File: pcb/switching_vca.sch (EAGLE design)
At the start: 38 parts, among them Q101 PMOS, Q102 NJFET, U101 LM319, U102 LF353D, U103 LF353D, U701 V_REG_LDOSMD

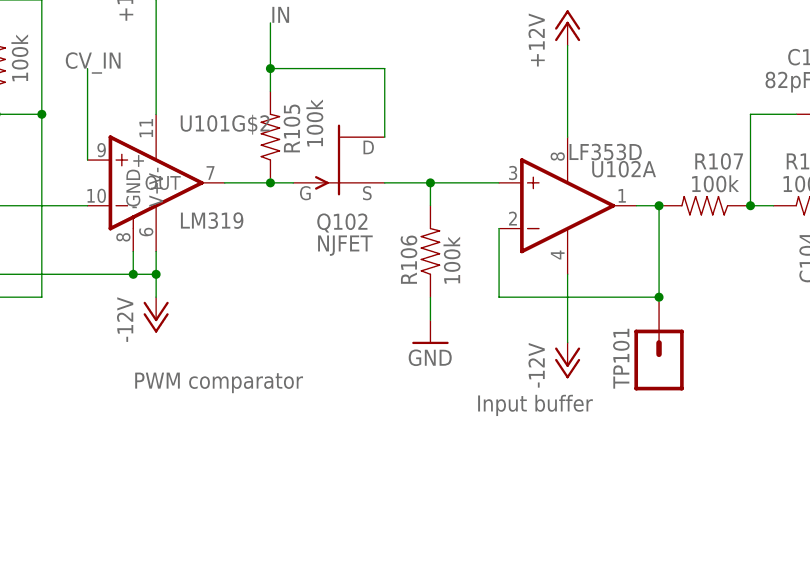
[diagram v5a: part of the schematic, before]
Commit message: added test point for PWM comparator output
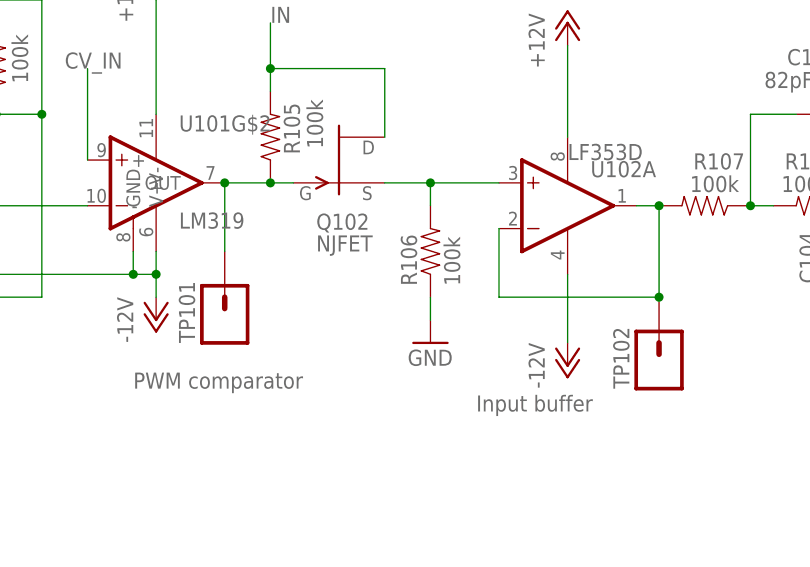
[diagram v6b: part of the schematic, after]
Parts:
- added TP102: M01PTH, SparkFun:M01PTH
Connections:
- net N$15: now also TP102.1; no longer TP101.1
- net N$3: now also TP101.1
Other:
- moved on the sheet: TP101
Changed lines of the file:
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@@
 <setting verticaltext="up"/>
 </settings>
-<grid distance="0.1" unitdist="inch" unit="inch" style="lines" multiple="1" display="yes" altdistance="0.01" altunitdist="inch" altunit="inch"/>
+<grid distance="0.1" unitdist="inch" unit="inch" style="lines" multiple="1" display="no" altdistance="0.01" altunitdist="inch" altunit="inch"/>
 <layers>
 <layer number="1" name="Top" color="4" fill="1" visible="no" active="no"/>
@@
 <part name="U701" library="SparkFun" deviceset="V_REG_LDO" device="SMD"/>
 <part name="U101" library="russruss" deviceset="LM319" device=""/>
+<part name="TP102" library="SparkFun" deviceset="M01" device="PTH" value=""/>
 <part name="TP101" library="SparkFun" deviceset="M01" device="PTH" value=""/>
 </parts>
@@
 <instance part="U101" gate="G$2" x="73.66" y="121.92"/>
 <instance part="U101" gate="G$3" x="73.66" y="121.92"/>
-<instance part="TP101" gate="G$1" x="129.54" y="101.6" rot="R90"/>
+<instance part="TP102" gate="G$1" x="129.54" y="101.6" rot="R90"/>
+<instance part="TP101" gate="G$1" x="81.28" y="106.68" rot="R90"/>
 </instances>
 <busses>
@@
 <pinref part="U101" gate="G$2" pin="OUT"/>
 <wire x1="81.28" y1="121.92" x2="86.36" y2="121.92" width="0.1524" layer="91"/>
+<pinref part="TP101" gate="G$1" pin="1"/>
+<wire x1="81.28" y1="121.92" x2="81.28" y2="114.3" width="0.1524" layer="91"/>
+<junction x="81.28" y="121.92"/>
 </segment>
 </net>
@@
 <wire x1="111.76" y1="116.84" x2="111.76" y2="109.22" width="0.1524" layer="91"/>
 <wire x1="111.76" y1="109.22" x2="129.54" y2="109.22" width="0.1524" layer="91"/>
-<pinref part="TP101" gate="G$1" pin="1"/>
+<pinref part="TP102" gate="G$1" pin="1"/>
 <junction x="129.54" y="109.22"/>
 </segment>
